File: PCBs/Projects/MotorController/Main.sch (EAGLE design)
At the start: 175 parts, among them Q1 ZXMP10A17GQ, Q2 MMBT5551LT1G, Q3 BUK9240-100A.118, Q4 BUK9240-100A.118, Q5 NCV8440, Q6 NCV8440, SW1 DIP-SWTCH-16POSCD16RM0SBR, U1 LT4356-2, U10 UCC27211A-Q1, U11 UCC27211A-Q1, U12 UCC27211A-Q1, U13 MTI85W100GC, U2 LT8631, U3 LT3045, U4 TMP101, U5 ACS758LCB, U6 ESDA6V1SC6Y, U7 ESDA6V1SC6Y, U8 ESDA6V1SC6Y, U9 ESDA6V1SC6Y

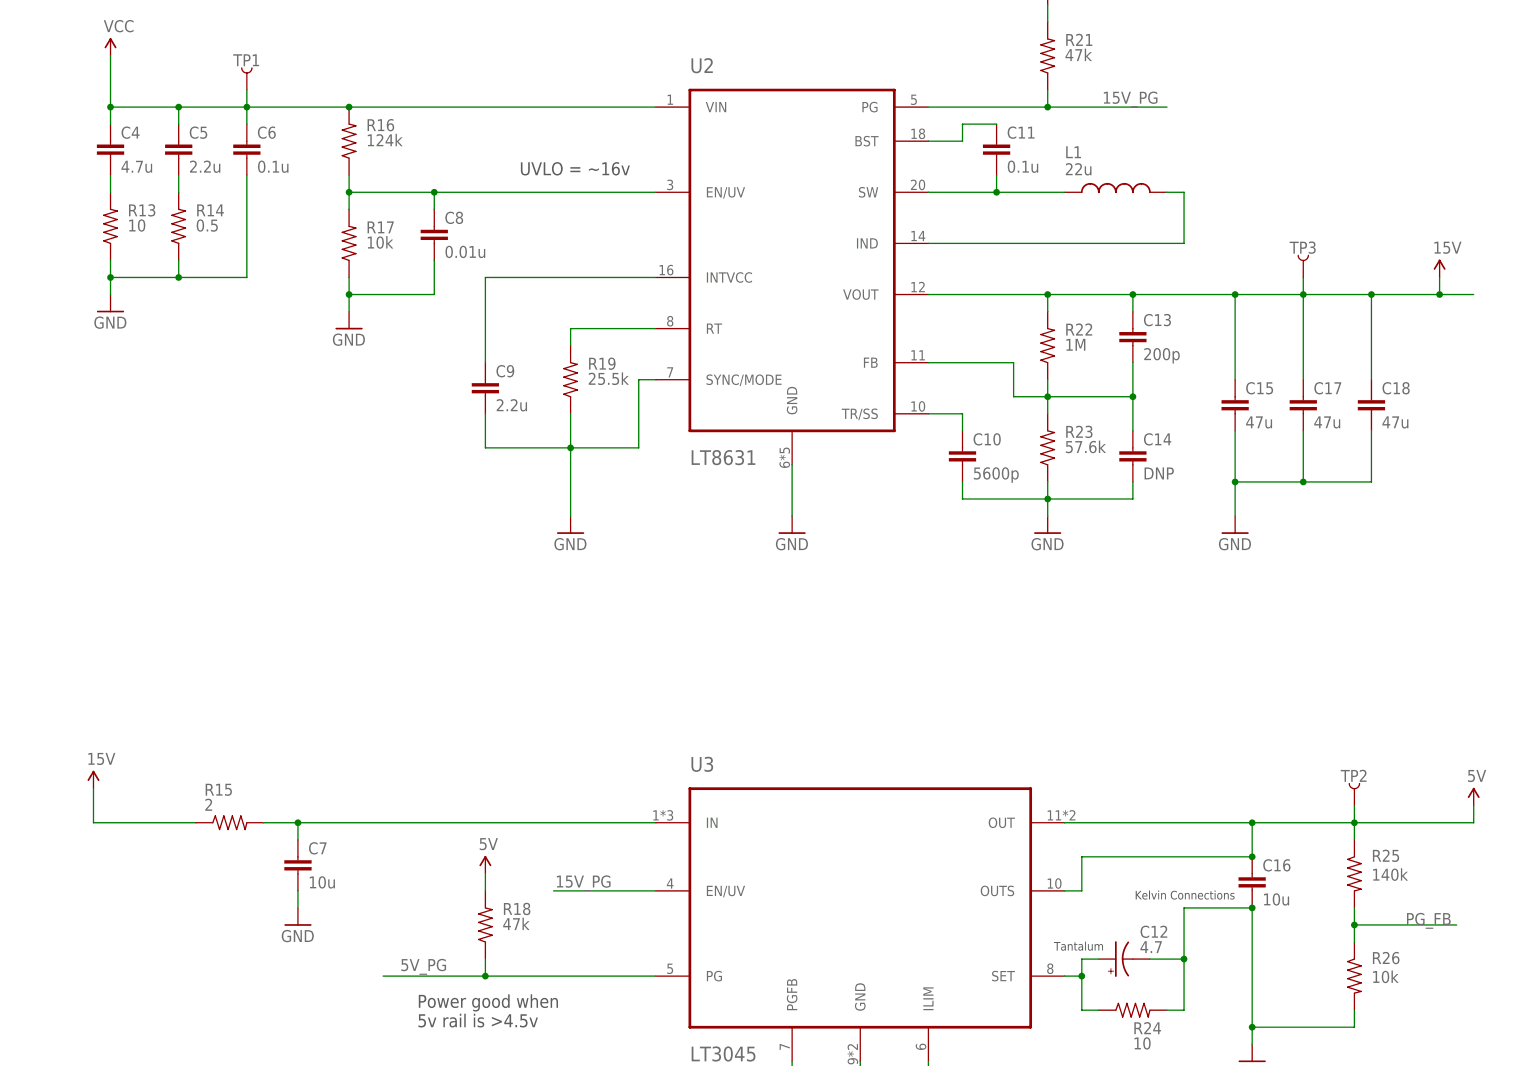
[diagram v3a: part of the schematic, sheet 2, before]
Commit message: switching psu layout 50% done
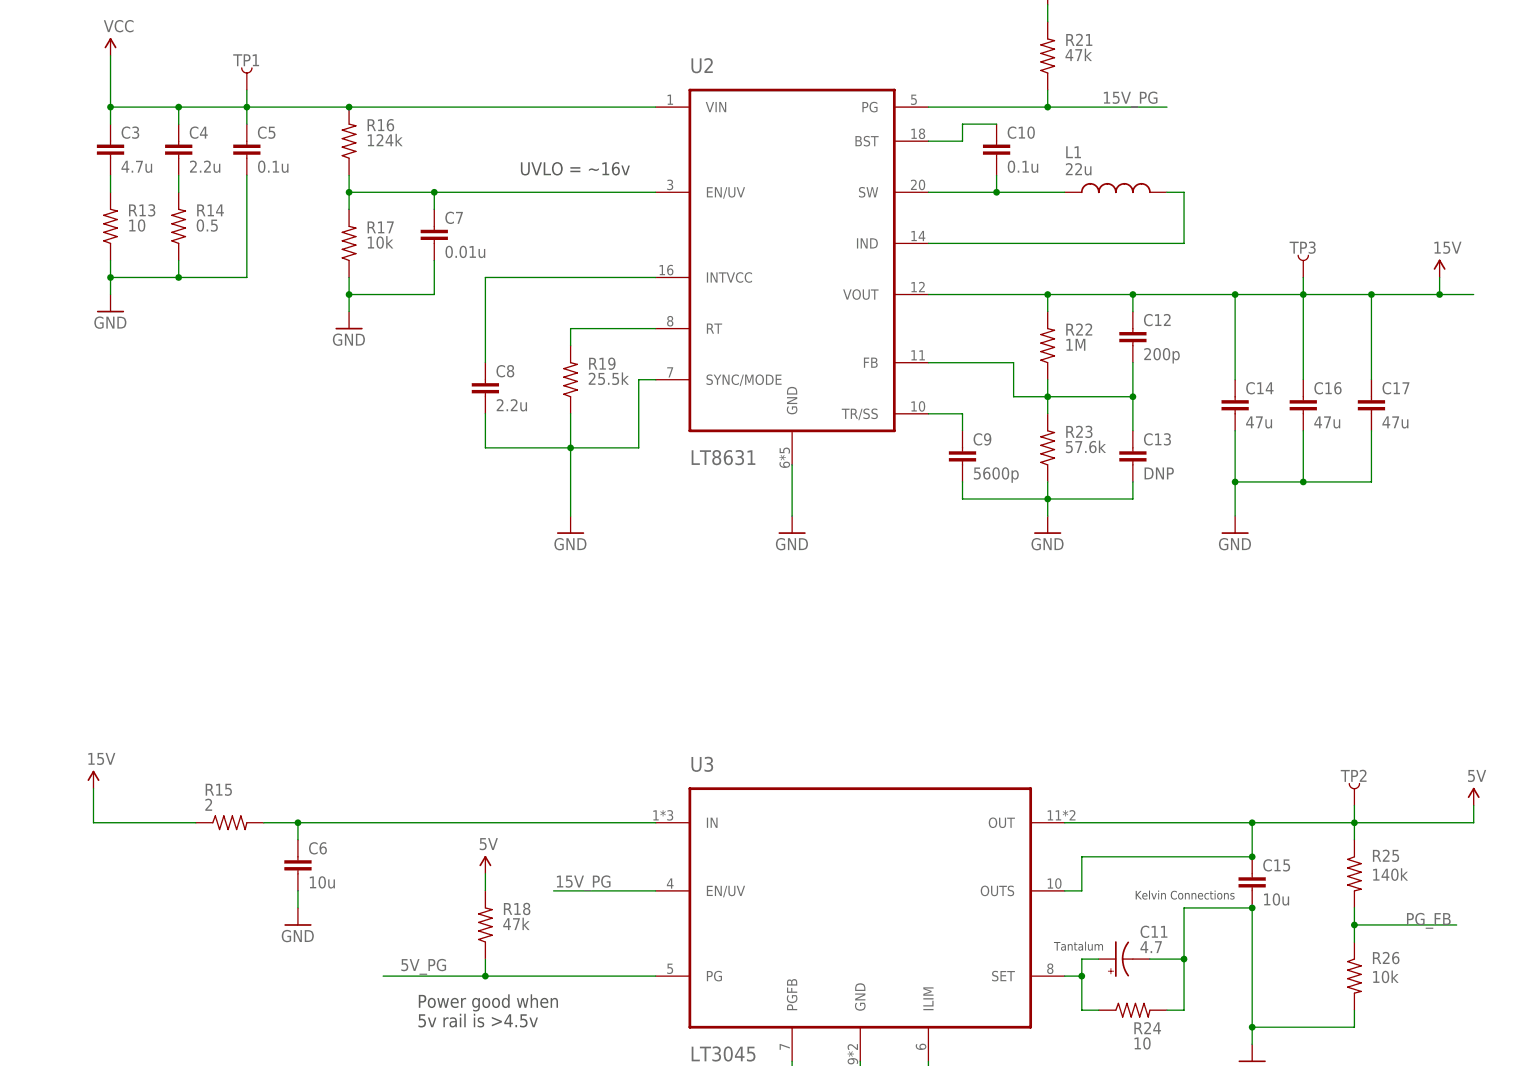
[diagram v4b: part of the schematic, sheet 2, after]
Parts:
- removed C35: 0.01u, SparkFun-Capacitors:CAP0805
- C10: value 5600p -> 0.1u; device SparkFun-Capacitors:CAP1210 -> SparkFun-Capacitors:CAP0805
- C11: value 0.1u -> 4.7; device SparkFun-Capacitors:CAP0805 -> SparkFun-Capacitors:CAP_POL1206
- C12: value 4.7 -> 200p; device SparkFun-Capacitors:CAP_POL1206 -> SparkFun-Capacitors:CAP0805
- C13: value 200p -> DNP
- C14: value DNP -> 47u; device SparkFun-Capacitors:CAP0805 -> SparkFun-Capacitors:CAP1210
- C15: value 47u -> 10u
- C16: value 10u -> 47u
- C18: value 47u -> 0.1u; device SparkFun-Capacitors:CAP1210 -> SparkFun-Capacitors:CAP0805
- C22, C34: value 0.1u -> 0.01u
- C26: value 0.01u -> 0.1u
- C27: value 0.1u -> 4.7u; device SparkFun-Capacitors:CAP0805 -> SparkFun-Capacitors:CAP1210
- C3: device SparkFun-Passives:CAP1210 -> SparkFun-Capacitors:CAP1210
- C30: value 4.7u -> 0.1u; device SparkFun-Capacitors:CAP1210 -> SparkFun-Capacitors:CAP0805
- C4: value 4.7u -> 2.2u
- C5: value 2.2u -> 0.1u; device SparkFun-Capacitors:CAP1210 -> SparkFun-Capacitors:CAP0805
- C6: value 0.1u -> 10u; device SparkFun-Capacitors:CAP0805 -> SparkFun-Capacitors:CAP1210
- C7: value 10u -> 0.01u; device SparkFun-Capacitors:CAP1210 -> SparkFun-Capacitors:CAP0805
- C8: value 0.01u -> 2.2u
- C9: value 2.2u -> 5600p; device SparkFun-Capacitors:CAP1210 -> SparkFun-Capacitors:CAP0805
- R8: device SparkFun-Resistors:RESISTOR2010 -> SparkFun-Resistors:RESISTOR1206
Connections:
- removed net 15V1: D9.C
- removed net 15V2: D8.C
- removed net GND1: D9.A
- removed net GND2: D8.A
- net !VIN-FAULT: now also MOD1.P1_6
- net 15V: now also C12.1, C14.1, C16.1, C27.1, D8.C, D9.C; no longer C13.1, C15.1, C18.1, C30.1
- net 5V: now also C15.1, C18.1, C22.1, C25.1, MOD1.VDD, MOD1.VDDIO; no longer C16.1, C21.1, C24.1, C27.1
- net 5V_SET_CONNECTION: now also C11.+; no longer C12.+
- net A: now also C30.2; no longer C31.2
- net B: now also C31.2; no longer C32.2
- net C: now also C32.2; no longer C33.2
- net GND: now also C11.-, C13.2, C24.2, C26.2, C33.2, C5.2, D8.A, D9.A, MOD1.GND; no longer C10.2, C12.-, C22.2, C25.2, C3.2, C30.2, C35.2
- net H1: now also C22.2; no longer C23.2
- net H2: now also C23.2; no longer C24.2
- net H3: now also C25.2; no longer C26.2
- net INH_A: now also MOD1.P2_3
- net INH_B: now also MOD1.P2_5
- net INH_C: now also MOD1.P2_7
- net INL_A: now also MOD1.P2_4
- net INL_B: now also MOD1.P2_6
- net INL_C: now also MOD1.P12_7
- net ISENSE: now also C24.1, MOD1.P0_5; no longer C25.1
- net MODESET1: now also R34.1
- net MODESET2: now also R35.1
- net N$12: now also C10.1; no longer C11.1
- net N$14: now also C7.1; no longer C8.1
- net N$15: now also C8.1; no longer C9.1
- net N$16: now also MOD1.P15_3
- net N$18: now also C9.1; no longer C10.1
- net N$2: now also C30.1; no longer C31.1
- net N$21: now also C12.2, C13.1; no longer C13.2, C14.1
- net N$24: now also C6.1; no longer C7.1
- net N$25: now also C3.2; no longer C4.2
- net N$26: now also C4.2; no longer C5.2
- net N$3: now also C31.1; no longer C32.1
- net N$31: now also C34.1; no longer C35.1
- net N$32: now also MOD1.P12_6
- net N$33: now also MOD1.P12_5
- net N$34: now also MOD1.P12_4
- net N$39: now also C21.1, MOD1.P3_5; no longer C22.1
- net N$41: now also MOD1.P1_7
- net N$42: now also MOD1.P12_3
- net N$43: now also MOD1.P1_4
- net N$44: now also MOD1.P1_5
- net N$47: now also MOD1.P12_1
- net N$48: now also MOD1.P12_2
- net N$49: now also MOD1.P2_0
- net N$5: now also C32.1; no longer C33.1
- net N$57: now also C33.1; no longer C34.1
- net N$6: now also C10.2; no longer C11.2
- net N$8: now also MOD1.P12_0
- net SCL: now also MOD1.P15_1
- net SDA: now also MOD1.P15_0
- net T_ALERT: now also MOD1.P15_2
- net VCC: no longer C6.1
- net VSENSE: now also MOD1.P0_1, TP9.1
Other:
- note added: "R8 = WSL1206R2000FEA"
- moved on the sheet: C10, C13, C14, C15, C16, C17, C19, C20, C21, C22, C23, C24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

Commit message: LDO placed and routed
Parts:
- R24: value 10 -> 49.9k
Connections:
- net 15V: no longer R28.2
- net 5V: now also R28.2
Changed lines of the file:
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@@
 <part name="U3" library="IC" deviceset="LT3045" device=""/>
 <part name="GND12" library="SparkFun-Aesthetics" deviceset="GND" device=""/>
-<part name="R24" library="SparkFun-Resistors" deviceset="RESISTOR" device="0805-RES" value="10"/>
+<part name="R24" library="SparkFun-Resistors" deviceset="RESISTOR" device="0805-RES" value="49.9k"/>
 <part name="C15" library="SparkFun-Capacitors" deviceset="CAP" device="1210" value="10u"/>
 <part name="GND15" library="SparkFun-Aesthetics" deviceset="GND" device=""/>
@@
 <part name="R28" library="SparkFun-Resistors" deviceset="RESISTOR" device="0805-RES" value="1k"/>
 <part name="D6" library="SparkFun-LED" deviceset="LED-RED" device="1206" value="GREEN"/>
-<part name="SUPPLY11" library="SparkFun-Aesthetics" deviceset="15V" device=""/>
 <part name="R18" library="SparkFun-Resistors" deviceset="RESISTOR" device="0805-RES" value="47k"/>
 <part name="SUPPLY6" library="SparkFun-Aesthetics" deviceset="5V" device=""/>
@@
 <part name="C9" library="SparkFun-Capacitors" deviceset="CAP" device="0805" value="5600p"/>
 <part name="C8" library="SparkFun-Capacitors" deviceset="CAP" device="0805" value="2.2u"/>
+<part name="SUPPLY11" library="SparkFun-Aesthetics" deviceset="5V" device=""/>
 </parts>
 <sheets>
@@
 </instance>
 <instance part="D6" gate="G$1" x="345.44" y="91.44"/>
-<instance part="SUPPLY11" gate="G$1(15V)" x="345.44" y="109.22"/>
 <instance part="R18" gate="G$1" x="152.4" y="76.2" smashed="yes" rot="R90">
 <attribute name="NAME" x="154.94" y="77.6986" size="1.778" layer="95"/>
@@
 <instance part="C9" gate="G$1" x="223.52" y="144.78"/>
 <instance part="C8" gate="G$1" x="152.4" y="154.94"/>
+<instance part="SUPPLY11" gate="G$1" x="345.44" y="109.22"/>
 </instances>
 <busses>
@@
 <pinref part="SUPPLY6" gate="G$1" pin="5V"/>
 <wire x1="152.4" y1="81.28" x2="152.4" y2="83.82" width="0.4064" layer="91"/>
+</segment>
+<segment>
+<pinref part="R28" gate="G$1" pin="2"/>
+<wire x1="345.44" y1="109.22" x2="345.44" y2="106.68" width="0.4064" layer="91"/>
+<pinref part="SUPPLY11" gate="G$1" pin="5V"/>
 </segment>
 </net>
@@
 <wire x1="345.44" y1="213.36" x2="345.44" y2="215.9" width="0.4064" layer="91"/>
 </segment>
-<segment>
-<pinref part="SUPPLY11" gate="G$1(15V)" pin="15V"/>
-<pinref part="R28" gate="G$1" pin="2"/>
-<wire x1="345.44" y1="109.22" x2="345.44" y2="106.68" width="0.4064" layer="91"/>
-</segment>
-</net>
+</net>

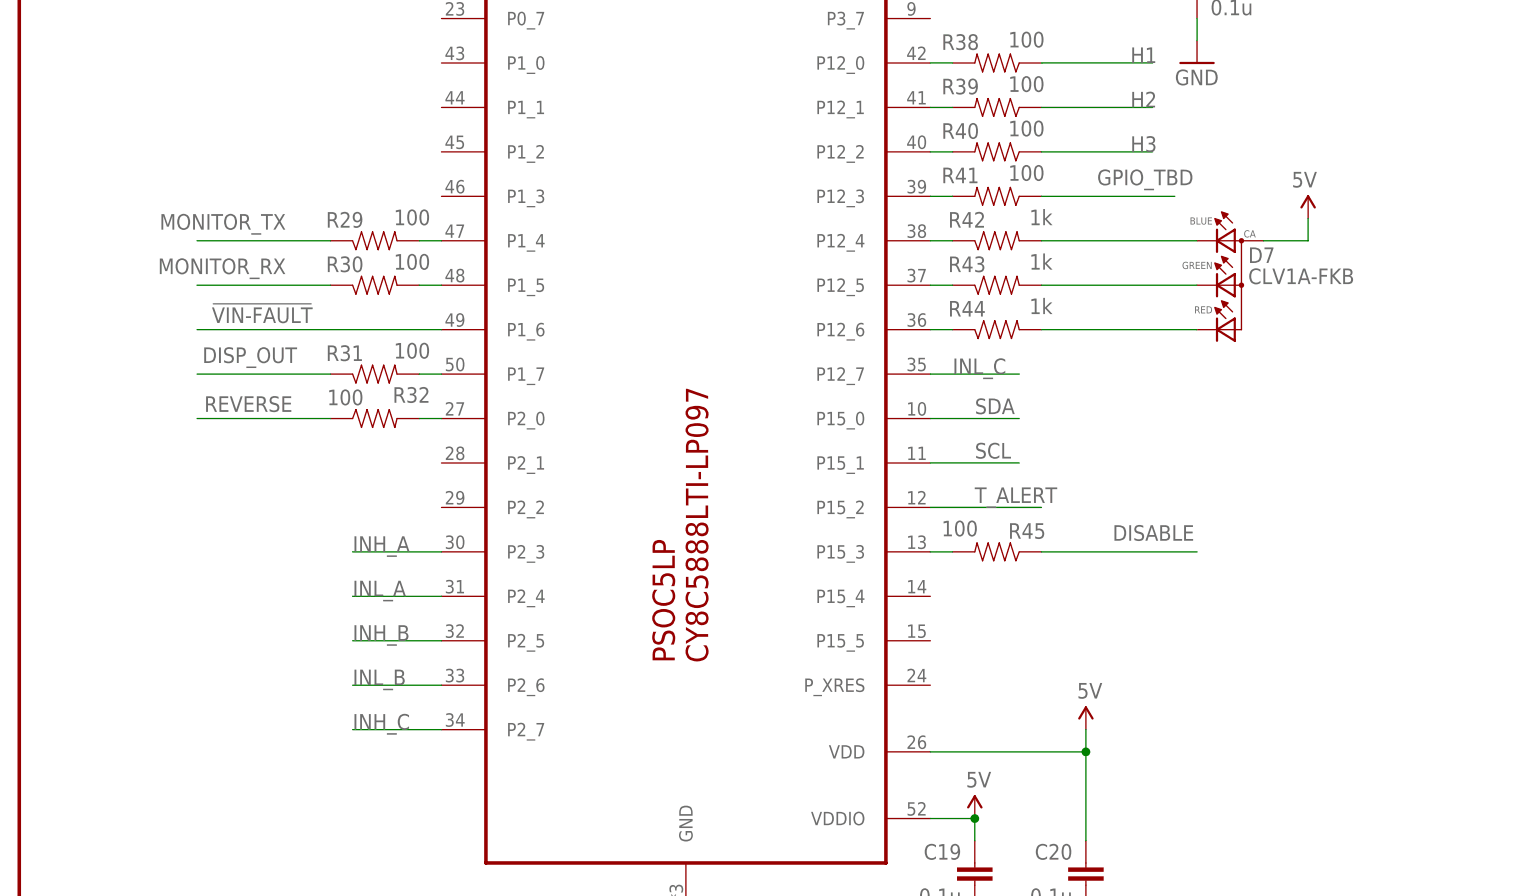
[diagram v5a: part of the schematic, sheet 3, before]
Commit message: Major layout work
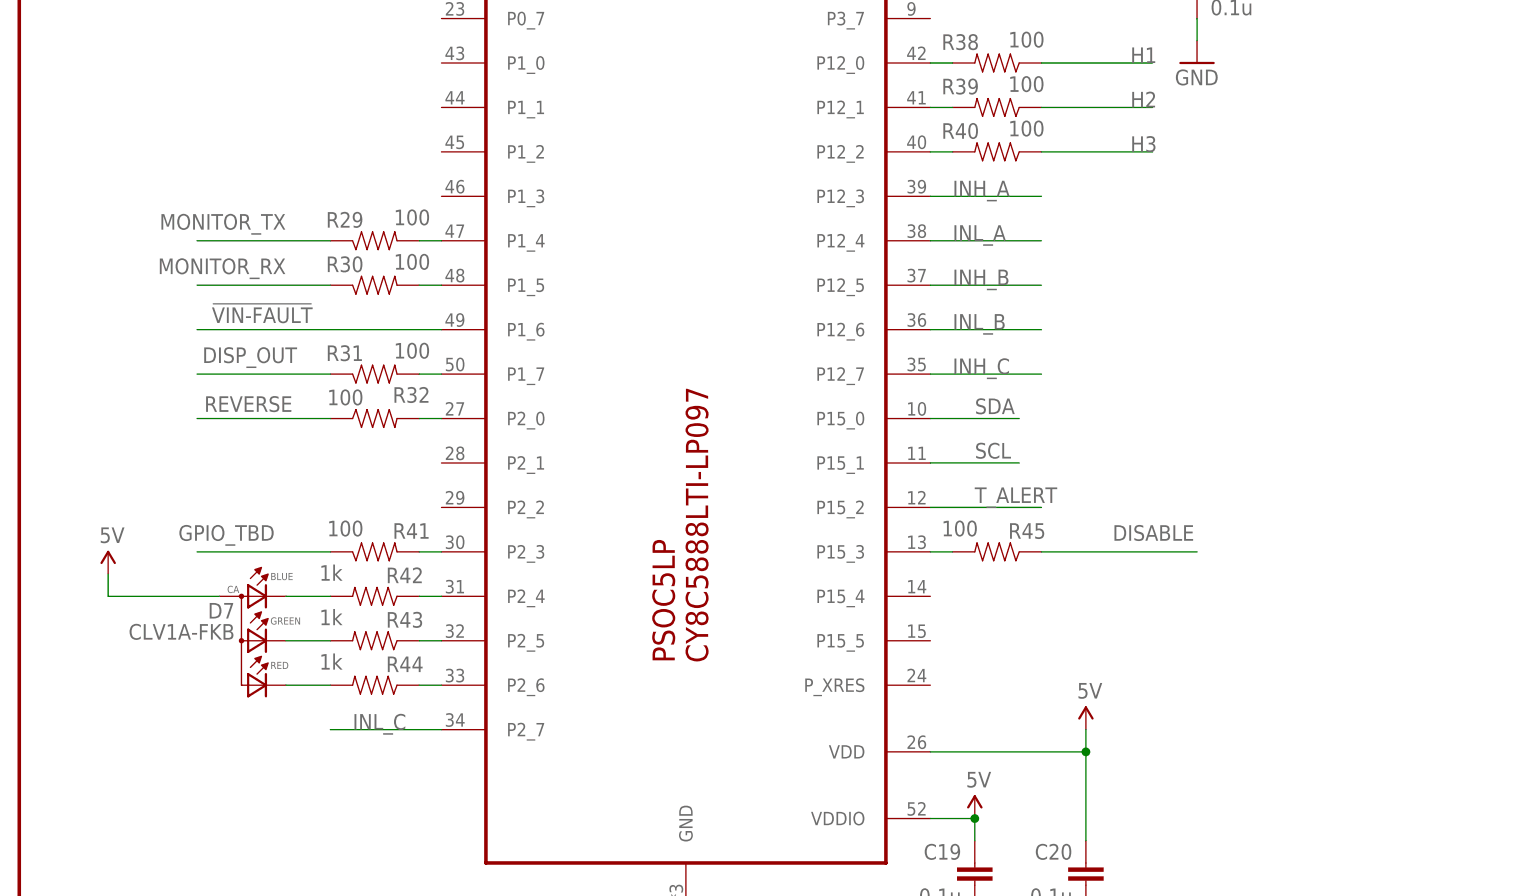
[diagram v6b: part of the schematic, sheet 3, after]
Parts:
- D10, D8, D9: value 1SMA15AT3G -> SZMM3Z18VST1G; device SparkFun-DiscreteSemi:TVSSMA -> SparkFun-DiscreteSemi:DIODE-ZENERSZMM3Z18VST1G
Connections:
- net INH_A: now also MOD1.P12_3; no longer MOD1.P2_3
- net INH_B: now also MOD1.P12_5; no longer MOD1.P2_5
- net INH_C: now also MOD1.P12_7; no longer MOD1.P2_7
- net INL_A: now also MOD1.P12_4; no longer MOD1.P2_4
- net INL_B: now also MOD1.P12_6; no longer MOD1.P2_6
- net INL_C: no longer MOD1.P12_7
- net N$32: now also MOD1.P2_6; no longer MOD1.P12_6
- net N$33: now also MOD1.P2_5; no longer MOD1.P12_5
- net N$34: now also MOD1.P2_4; no longer MOD1.P12_4
- net N$42: now also MOD1.P2_3; no longer MOD1.P12_3
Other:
- moved on the sheet: D7, R41, R42, R43, R44

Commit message: More signals run
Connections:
- net INL_C: now also MOD1.P2_7
- net REVERSE: now also U6.IO2; no longer U6.IO3
- net THROTTLE_2: now also U6.IO3; no longer U6.IO2
- net VSENSE: now also U7.IO2; no longer U7.IO1
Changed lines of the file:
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@@
 </segment>
 <segment>
-<pinref part="U7" gate="G$1" pin="IO1"/>
-<wire x1="373.38" y1="251.46" x2="388.62" y2="251.46" width="0.4064" layer="91"/>
+<pinref part="U7" gate="G$1" pin="IO2"/>
+<wire x1="373.38" y1="246.38" x2="388.62" y2="251.46" width="0.4064" layer="91"/>
 <label x="378.46" y="251.46" size="1.778" layer="95"/>
 </segment>
@@
 <label x="281.94" y="34.29" size="1.778" layer="95"/>
 <junction x="264.16" y="33.02"/>
-<pinref part="U6" gate="G$1" pin="IO2"/>
-<wire x1="264.16" y1="33.02" x2="233.68" y2="33.02" width="0.4064" layer="91"/>
+<pinref part="U6" gate="G$1" pin="IO3"/>
+<wire x1="264.16" y1="33.02" x2="233.68" y2="27.94" width="0.4064" layer="91"/>
 </segment>
 <segment>
@@
 <net name="REVERSE" class="0">
 <segment>
-<pinref part="U6" gate="G$1" pin="IO3"/>
-<wire x1="233.68" y1="27.94" x2="251.46" y2="27.94" width="0.4064" layer="91"/>
+<pinref part="U6" gate="G$1" pin="IO2"/>
+<wire x1="233.68" y1="33.02" x2="251.46" y2="27.94" width="0.4064" layer="91"/>
 <label x="240.284" y="28.702" size="1.778" layer="95"/>
 </segment>
@@
 <label x="38.1" y="132.08" size="1.778" layer="95"/>
 <wire x1="35.56" y1="132.08" x2="48.26" y2="132.08" width="0.4064" layer="91"/>
-</segment>
-</net>
+<pinref part="MOD1" gate="G$1" pin="P2_7"/>
+</segment>
+</net>
